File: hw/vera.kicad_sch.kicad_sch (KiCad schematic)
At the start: 36 parts, among them J4 VGA D15, U18 VERAduino, U19 74HCT00, U20 TXS0108EPW, U21 TXS0108EPW

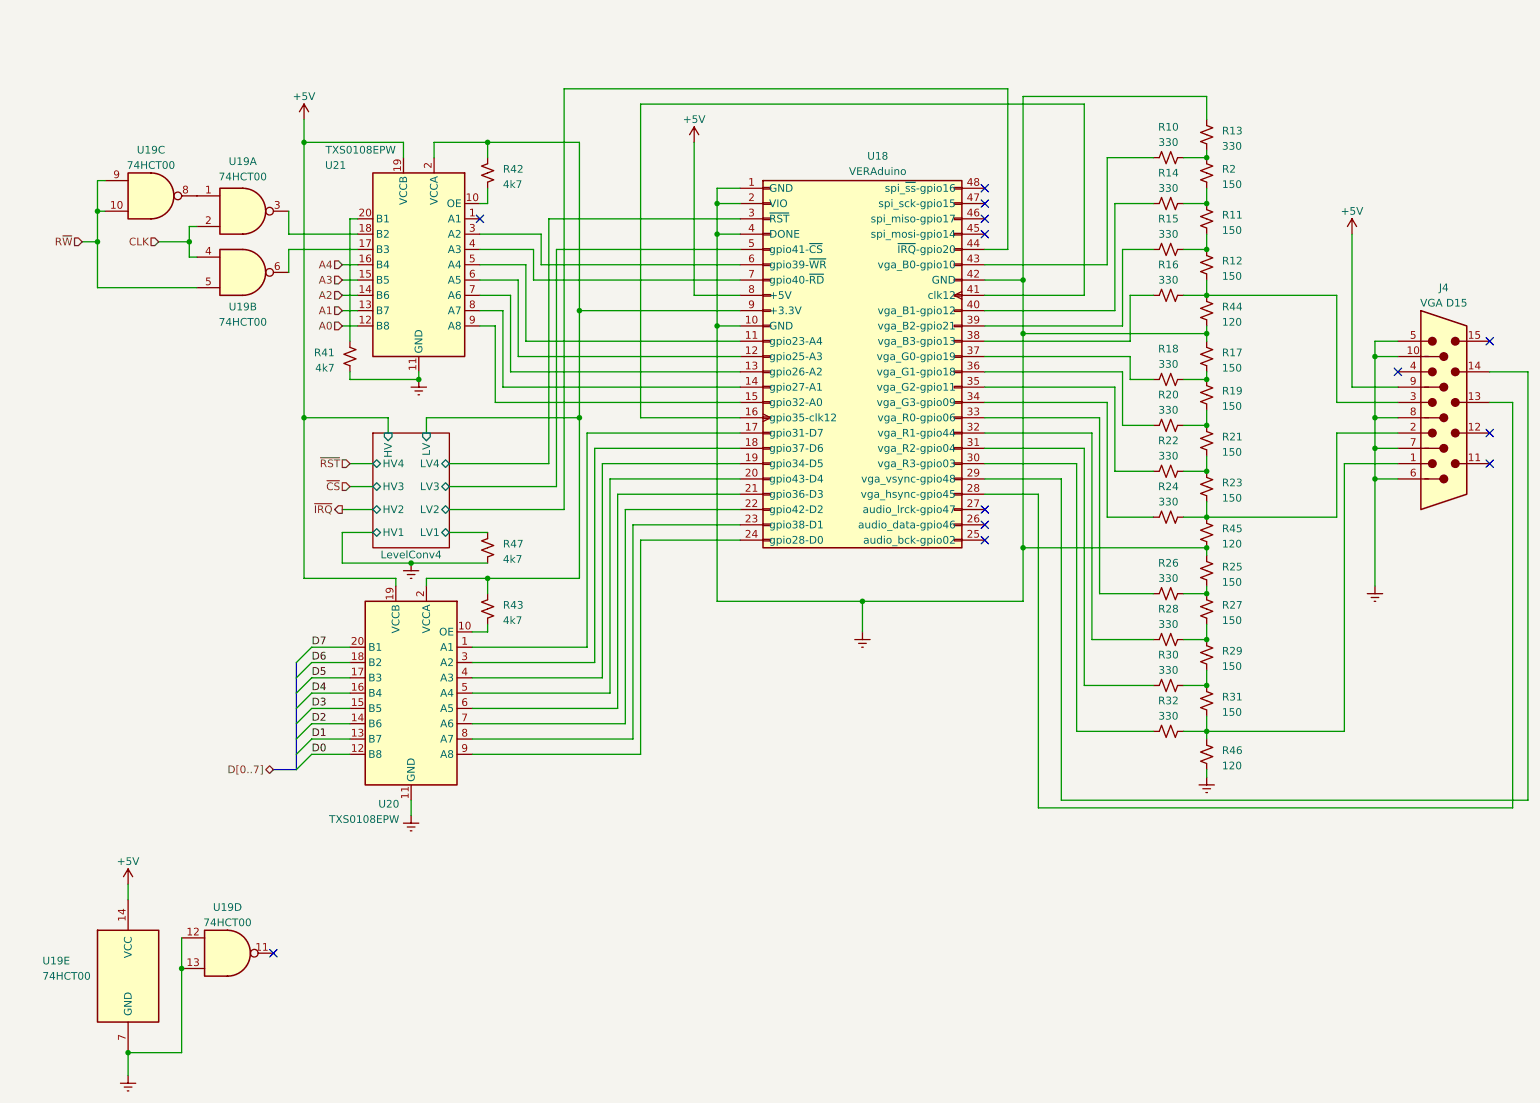
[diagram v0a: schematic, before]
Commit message: add hw schematics for video output with veraduino
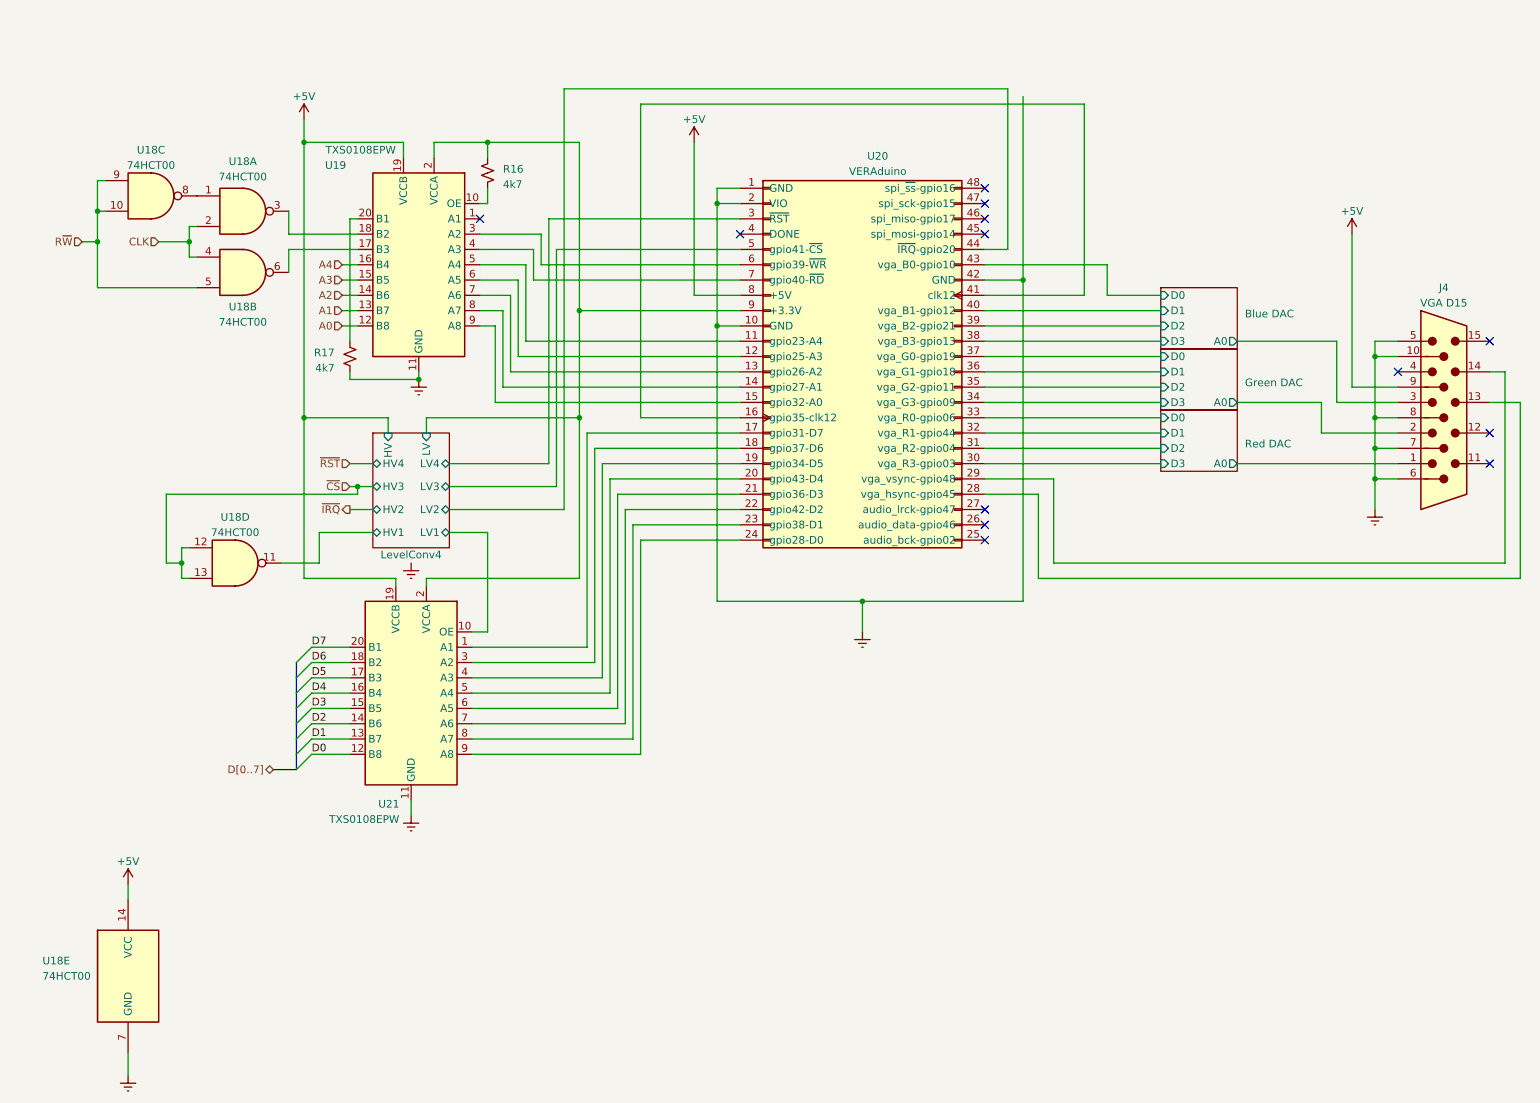
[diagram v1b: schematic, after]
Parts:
- removed R10, R13, R14, R15, R16, R18, R20, R22, R24, R26, R28, R30, R32: 330, symbol Device:R_Small_US
- removed R11, R12, R17, R19, R2, R21, R23, R25, R27, R29, R31: 150, symbol Device:R_Small_US
- removed R43, R47: 4k7, symbol Device:R_Small_US
- removed R44, R45, R46: 120, symbol Device:R_Small_US
- renumbered R42 to R16, R41 to R17, U19 to U18, U21 to U19, U18 to U20, U20 to U21
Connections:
- net Earth: no longer U18.12, U18.13, U20.4 (DONE)
- net LevelConv4/LV1: now also U21.10 (OE)
- net ~{CS}: now also U18.12, U18.13
- net Blue DAC/D0: now reaches U20.43 (vga_B0-gpio10)
- net Blue DAC/D2: now reaches U20.39 (vga_B2-gpio21)
- net Green DAC/D2: now reaches U20.35 (vga_G2-gpio11)
- net Green DAC/D3: now reaches U20.34 (vga_G3-gpio09)
- net Green DAC/A0: now reaches J4.2
- net Red DAC/D3: now reaches U20.30 (vga_R3-gpio03)
- net Red DAC/A0: now reaches J4.1
- net Blue DAC/A0: now reaches J4.3
- net Red DAC/D2: now reaches U20.31 (vga_R2-gpio04)
- net Red DAC/D1: now reaches U20.32 (vga_R1-gpio44)
- net Red DAC/D0: now reaches U20.33 (vga_R0-gpio06)
- net Green DAC/D1: now reaches U20.36 (vga_G1-gpio18)
- net Green DAC/D0: now reaches U20.37 (vga_G0-gpio19)
- net Blue DAC/D3: now reaches U20.38 (vga_B3-gpio13)
- net Blue DAC/D1: now reaches U20.40 (vga_B1-gpio12)
- net LevelConv4/HV1: now reaches U18.11
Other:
- added sheet Blue DAC (video_dac.kicad_sch)
- added sheet Green DAC (video_dac.kicad_sch)
- added sheet Red DAC (video_dac.kicad_sch)
- moved on the sheet: U18D

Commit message: clean up hw schematics
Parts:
- removed R16, R17: 4k7, symbol Device:R_Small_US
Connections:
- net A0: now also U19.17 (B3), U19.4 (A3), U20.15 (gpio32-A0); no longer U19.12 (B8)
- net A1: now also U19.16 (B4), U19.5 (A4), U20.14 (gpio27-A1); no longer U19.13 (B7)
- net A2: now also U19.15 (B5), U19.6 (A5), U20.13 (gpio26-A2); no longer U19.14 (B6)
- net A3: now also U19.14 (B6), U19.7 (A6), U20.12 (gpio25-A3); no longer U19.15 (B5)
- net A4: now also U19.13 (B7), U19.8 (A7), U20.11 (gpio23-A4); no longer U19.16 (B4)
- net D0: now also U20.24 (gpio28-D0), U21.1 (A1), U21.20 (B1); no longer U21.12 (B8)
- net D1: now also U20.23 (gpio38-D1), U21.18 (B2), U21.3 (A2); no longer U21.13 (B7)
- net D2: now also U20.22 (gpio42-D2), U21.17 (B3), U21.4 (A3); no longer U21.14 (B6)
- net D3: now also U20.21 (gpio36-D3), U21.16 (B4), U21.5 (A4); no longer U21.15 (B5)
- net D4: now also U20.20 (gpio43-D4), U21.15 (B5), U21.6 (A5); no longer U21.16 (B4)
- net D5: now also U20.19 (gpio34-D5), U21.14 (B6), U21.7 (A6); no longer U21.17 (B3)
- net D6: now also U20.18 (gpio37-D6), U21.13 (B7), U21.8 (A7); no longer U21.18 (B2)
- net D7: now also U20.17 (gpio31-D7), U21.12 (B8), U21.9 (A8); no longer U21.20 (B1)
- net Earth: now also U19.20 (B1)
- net LevelConv4/HV1: now also U18.6; no longer U18.11
- net LevelConv4/LV: now also U19.10 (OE)
- net LevelConv4/LV1: now also U20.7 (gpio40-~{RD}); no longer U21.10 (OE)
- net LevelConv4/LV2: now also U20.6 (gpio39-~{WR}); no longer U20.44 (~{IRQ}-gpio20)
- net ~{IRQ}: now also U19.12 (B8)
- net at U19.18 (B2): now also U18.11; no longer U18.3
- net at U19.9 (A8): now also U20.44 (~{IRQ}-gpio20); no longer U20.15 (gpio32-A0)
- net at U19.3 (A2): now also U21.10 (OE); no longer U20.6 (gpio39-~{WR})
- new net LevelConv4/HV2: U18.3
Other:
- note added: "~{RD}"
- note added: "~{WR}"
- moved on the sheet: U18A, U18B, U18C, U18D, U19, U21
